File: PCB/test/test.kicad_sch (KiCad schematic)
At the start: 52 parts, among them CN1 HEADER_1X10, CN2 HEADER_1X10, CN3 USB_1, CN4 HEADER_1X4, CN5 UFL, SW2 MLL1200S_TE, U1 STM32WBxx_QFN48, U2 USBLC6-2SC6, U3 LD3985M33R, X1 NX2016_32MHz, X2 NX2012_32K768Hz

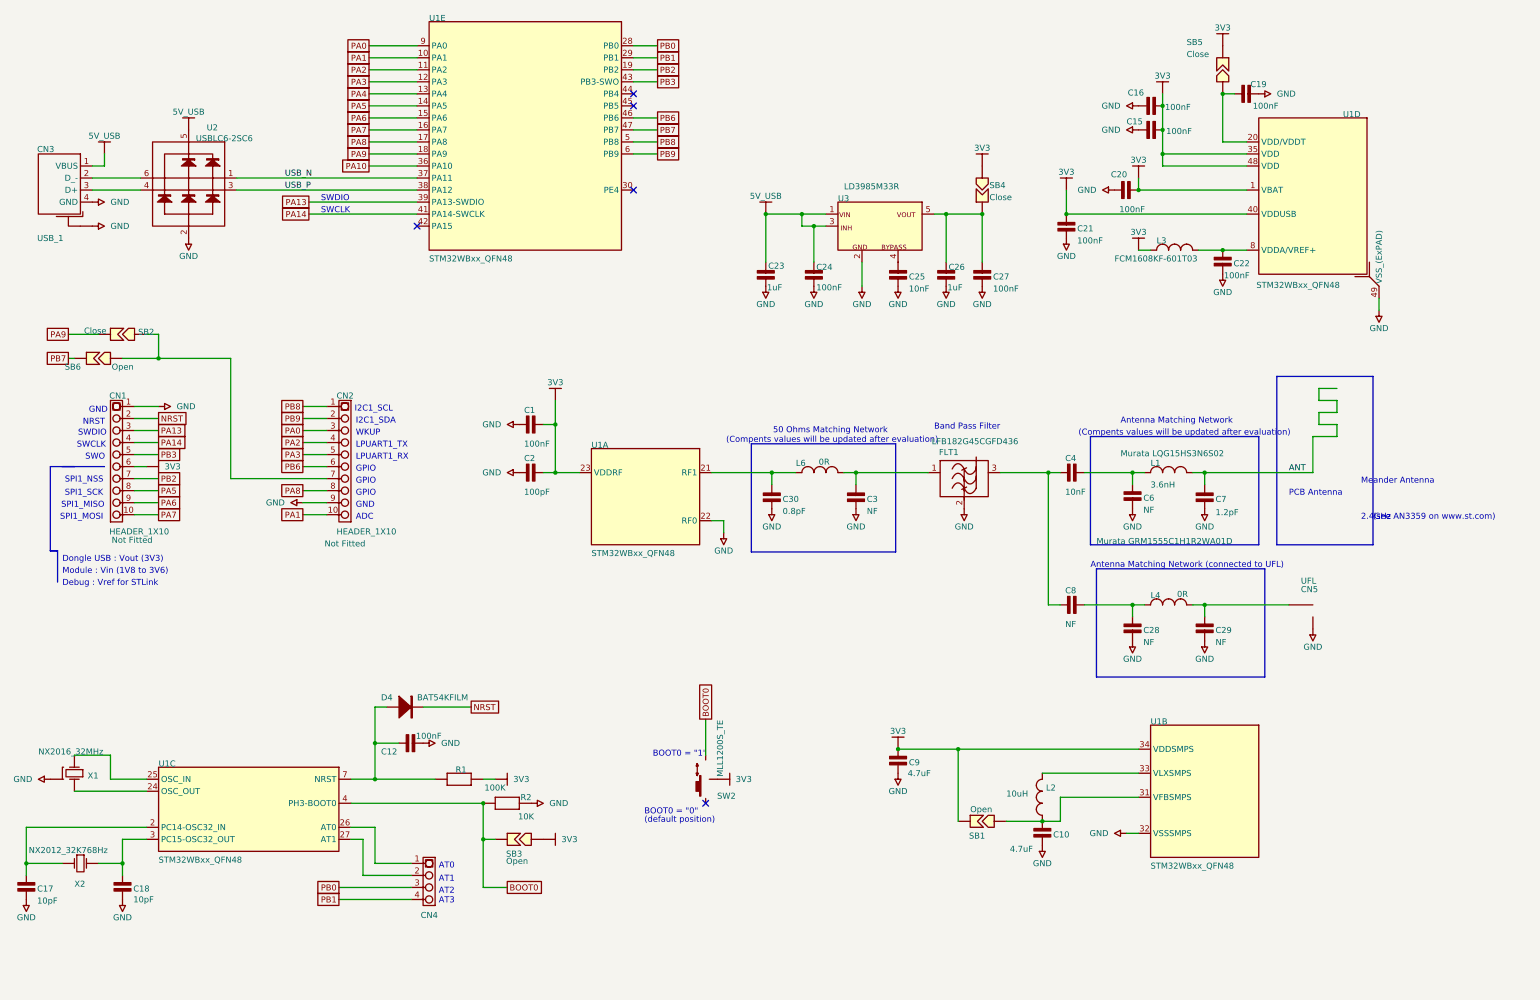
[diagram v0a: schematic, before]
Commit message: ajout de test
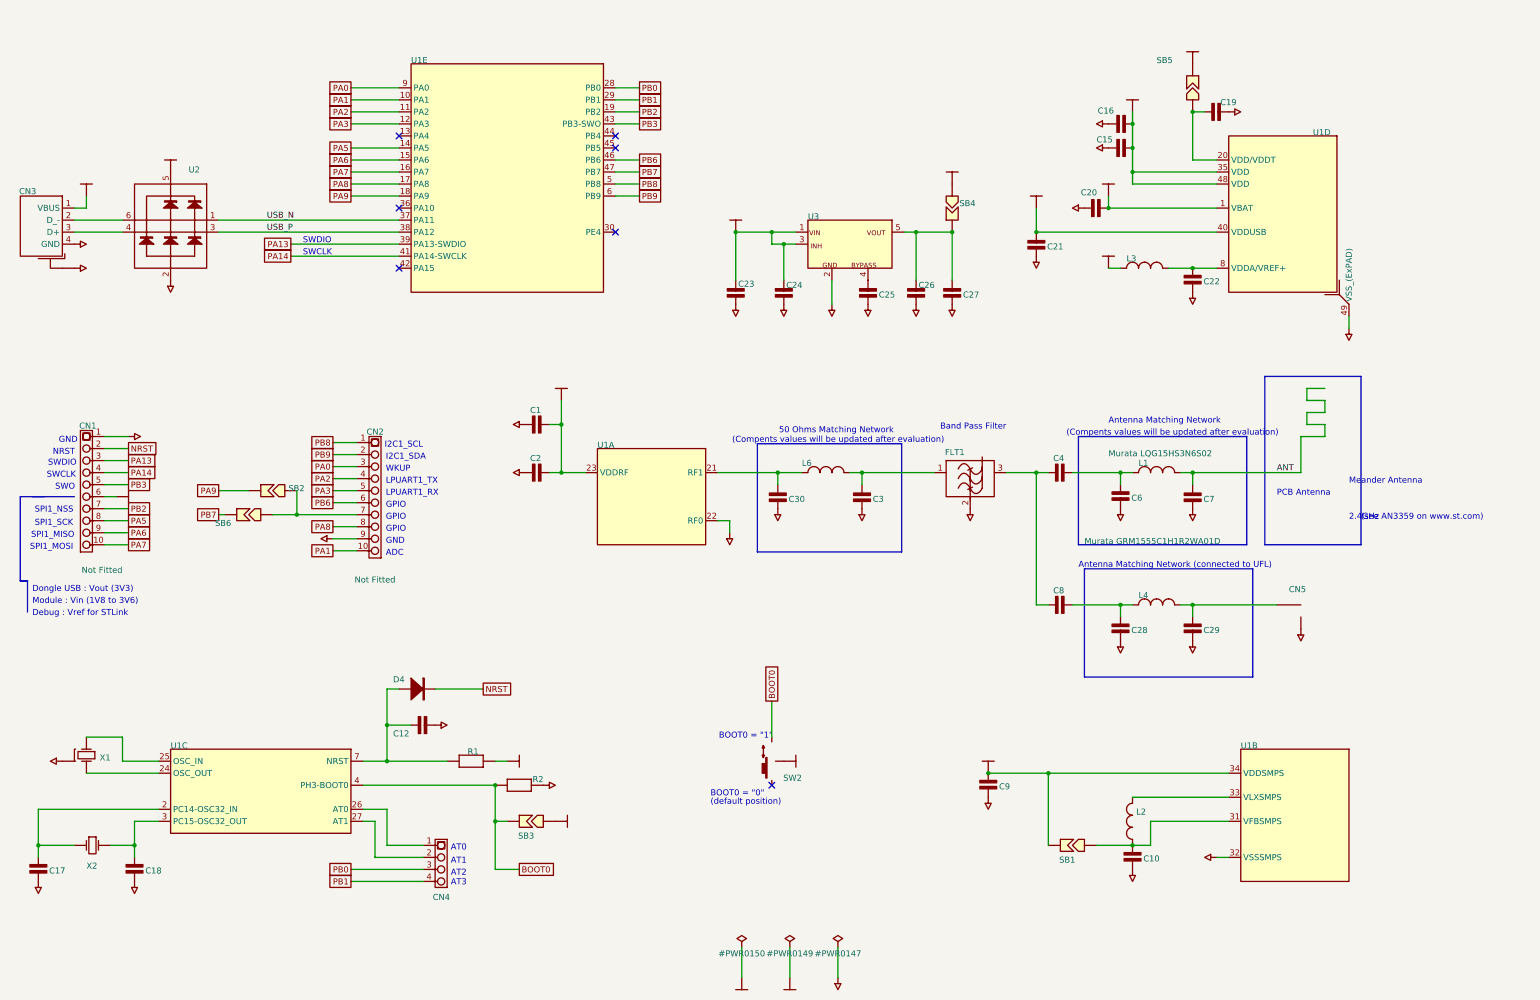
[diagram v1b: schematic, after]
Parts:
- removed C1, C12, C19, C20: 100nF, 0402_CAP_NPOL, symbol Schematic-altium-import:1_CAP_NPOL
- removed C10, C9: 4.7uF, 0402_CAP_NPOL, symbol Schematic-altium-import:0_CAP_NPOL
- removed C15, C16: 100nF, 0402_CAP_NPOL, symbol Schematic-altium-import:3_CAP_NPOL
- removed C17, C18: 10pF, 0402_CAP_NPOL, symbol Schematic-altium-import:0_CAP_NPOL
- removed C2: 100pF, 0402_CAP_NPOL, symbol Schematic-altium-import:1_CAP_NPOL
- removed C21, C24, C27: 100nF, 0402_CAP_NPOL, symbol Schematic-altium-import:2_CAP_NPOL
- removed C22: 100nF, 0402_CAP_NPOL, symbol Schematic-altium-import:0_CAP_NPOL
- removed C23, C26: 1uF, 0603_CAP_NPOL, symbol Schematic-altium-import:2_CAP_NPOL
- removed C25: 10nF, 0402_CAP_NPOL, symbol Schematic-altium-import:2_CAP_NPOL
- removed C28, C29, C6: NF, 0402_CAP_NPOL, symbol Schematic-altium-import:0_CAP_NPOL
- removed C3: NF, 0402_CAP_NPOL, symbol Schematic-altium-import:2_CAP_NPOL
- removed C30: 0.8pF, 0402_CAP_NPOL, symbol Schematic-altium-import:2_CAP_NPOL
- removed C4: 10nF, 0402_CAP_NPOL, symbol Schematic-altium-import:1_CAP_NPOL
- removed C7: 1.2pF, 0402_CAP_NPOL, symbol Schematic-altium-import:2_CAP_NPOL
- removed C8: NF, 0402_CAP_NPOL, symbol Schematic-altium-import:1_CAP_NPOL
- removed CN1: HEADER_1X10, Header M/F 1x10x2.54 NF, symbol Schematic-altium-import:0_HEADER_1X10
- removed CN2: HEADER_1X10, Header M/F 1x10x2.54 NF, symbol Schematic-altium-import:0_mirrored_HEADER_1X10
- removed CN3: USB_1, USB/A_M1, symbol Schematic-altium-import:0_USB_1
- removed CN4: HEADER_1X4, SIL4_127_B, symbol Schematic-altium-import:0_mirrored_HEADER_1X4
- removed CN5: UFL, UFL, symbol Schematic-altium-import:0_mirrored_UFL
- removed D4: BAT54KFILM, SOD523, symbol Schematic-altium-import:0_BAT54K
- removed FLT1: LFB182G45CGFD436, LFB182G45CGFD436, symbol Schematic-altium-import:0_LFB182G45CGFD436
- removed L1: 3.6nH, 0402_COIL, symbol Schematic-altium-import:1_INDUCTOR_SMD_STDL
- removed L2: 10uH, 0805_COIL, symbol Schematic-altium-import:2_IND_74479777310A
- removed L3: FCM1608KF-601T03, 0603_COIL, symbol Schematic-altium-import:1_IND_FCM1608KF-601T03
- removed L4, L6: 0R, 0402_COIL, symbol Schematic-altium-import:1_INDUCTOR_SMD_STDL
- removed R1: 100K, 0402_RES, symbol Schematic-altium-import:2_RES
- removed R2: 10K, 0402_RES, symbol Schematic-altium-import:0_RES
- removed SB1, SB3, SB6: Open, SB-tiny, symbol Schematic-altium-import:0_Strap2
- removed SB2: Close, SB-tiny, symbol Schematic-altium-import:0_Strap2
- removed SB4: Close, SB-tiny, symbol Schematic-altium-import:1_Strap2
- removed SB5: Close, SB-tiny, symbol Schematic-altium-import:3_Strap2
- removed SW2: MLL1200S_TE, MLL1200S_TE, symbol Schematic-altium-import:3_mirrored_MLL1200S_TE
- removed unit 5 of U1
- removed unit 4 of U1
- removed unit 3 of U1
- removed unit 1 of U1
- removed U2: USBLC6-2SC6, SOT23-6, symbol Schematic-altium-import:0_mirrored_USBLC6-2
- removed U3: LD3985M33R, SOT23-5, symbol Schematic-altium-import:0_LD3985M33R
- removed X1: NX2016_32MHz, NX2016_4P, symbol Schematic-altium-import:3_NX2016_32M
- removed X2: NX2012_32K768Hz, NX2012_2P, symbol Schematic-altium-import:0_NX2012_32K768
- added C1, C12, C19, C2, C20, C4, C8: (no value), symbol test-altium-import:1_CAP_NPOL
- added C10, C17, C18, C22, C28, C29, C6, C9: (no value), symbol test-altium-import:0_CAP_NPOL
- added C15, C16: (no value), symbol test-altium-import:3_CAP_NPOL
- added C21, C23, C24, C25, C26, C27, C30, C7: (no value), symbol test-altium-import:2_CAP_NPOL
- added CN1: (no value), symbol test-altium-import:0_HEADER_1X10
- added CN2: (no value), symbol test-altium-import:0_mirrored_HEADER_1X10
- added CN3: (no value), symbol test-altium-import:0_USB_1
- added CN4: (no value), symbol test-altium-import:0_mirrored_HEADER_1X4
- added CN5: (no value), symbol test-altium-import:0_mirrored_UFL
- added D4: (no value), symbol test-altium-import:0_BAT54K
- added FLT1: (no value), symbol test-altium-import:0_LFB182G45CGFD436
- added L1, L4, L6: (no value), symbol test-altium-import:1_INDUCTOR_SMD_STDL
- added L2: (no value), symbol test-altium-import:2_IND_74479777310A
- added L3: (no value), symbol test-altium-import:1_IND_FCM1608KF-601T03
- added R1: (no value), symbol test-altium-import:2_RES
- added R2: (no value), symbol test-altium-import:0_RES
- added SB1, SB2, SB3, SB6: (no value), symbol test-altium-import:0_Strap2
- added SB4: (no value), symbol test-altium-import:1_Strap2
- added SB5: (no value), symbol test-altium-import:3_Strap2
- added SW2: (no value), symbol test-altium-import:3_mirrored_MLL1200S_TE
- added U1: (no value), symbol test-altium-import:0_STM32WBxx_QFN48
- added U2: (no value), symbol test-altium-import:0_mirrored_USBLC6-2
- added U3: (no value), symbol test-altium-import:0_LD3985M33R
- added X1: (no value), symbol test-altium-import:3_NX2016_32M
- added X2: (no value), symbol test-altium-import:0_NX2012_32K768
- C3: renamed from U1; value STM32WBxx_QFN48 -> (none); footprint STM32WBxx_QFN48 -> (none); symbol Schematic-altium-import:0_STM32WBxx_QFN48 -> test-altium-import:2_CAP_NPOL
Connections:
- net 3V3: now also C1.2, C15.1, C16.1, C2.2, C20.2, C21.2, C9.1, CN1.6, L3.1, R1.1, SB1.2, SB3.1, SB4.1, SB5.2, SW2.2, U1.1 (VBAT), U1.23 (VDDRF), U1.34 (VDDSMPS), U1.35 (VDD), U1.40 (VDDUSB), U1.48 (VDD); no longer C3.34 (VDDSMPS)
- net 5V_USB: now also C23.2, C24.2, CN3.1 (VBUS), U2.5, U3.1 (VIN), U3.3 (CE)
- net ANT: now also C7.2, L1.2
- net BOOT0: now also R2.1, SB3.2, SW2.3, U1.4 (PH3-BOOT0)
- net GND: now also C3.1, C1.1, C10.2, C12.2, C15.2, C16.2, C17.2, C18.2, C19.2, C2.1, C20.1, C21.1, C22.2, C23.1, C24.1, C25.1, C26.1, C27.1, C28.2, C29.2, C30.1, C6.2, C7.1, C9.2, CN1.1, CN2.9, CN3.0 (Shield), CN3.4 (GND), CN5.2 (Y), FLT1.2 (GND), R2.2, U1.22 (RF0), U1.32 (VSSSMPS), U1.49 (VSS_(ExPAD)), U2.2, U3.2 (VSS), X1.2, X1.4; no longer C3.32 (VSSSMPS)
- net NRST: now also CN1.2, D4.K
- net PA0: now also CN2.3, U1.9 (PA0)
- net PA1: now also CN2.10, U1.10 (PA1)
- net PA13: now also CN1.3, U1.39 (PA13-SWDIO)
- net PA14: now also CN1.4, U1.41 (PA14-SWCLK)
- net PA2: now also CN2.4, U1.11 (PA2)
- net PA3: now also CN2.5, U1.12 (PA3)
- net PA5: now also CN1.8, U1.14 (PA5)
- net PA6: now also CN1.9, U1.15 (PA6)
- net PA7: now also CN1.10, U1.16 (PA7)
- net PA8: now also CN2.8, U1.17 (PA8)
- net PA9: now also SB2.2, U1.18 (PA9)
- net PB0: now also CN4.3, U1.28 (PB0)
- net PB1: now also CN4.4, U1.29 (PB1)
- net PB2: now also CN1.7, U1.19 (PB2)
- net PB3: now also CN1.5, U1.43 (PB3-SWO)
- net PB6: now also CN2.6, U1.46 (PB6)
- net PB7: now also SB6.2, U1.47 (PB7)
- net PB8: now also CN2.1, U1.5 (PB8)
- net PB9: now also CN2.2, U1.6 (PB9)
- net USB_N: now also U1.37 (PA11), U2.1
- net USB_P: now also U1.38 (PA12), U2.3
- new net: C29.1, CN5.1 (X), L4.2
- new net: C10.1, L2.1, SB1.1, U1.31 (VFBSMPS)
- new net: CN4.1, U1.26 (AT0)
- new net: CN4.2, U1.27 (AT1)
- new net: C3.2, FLT1.1 (I/O), L6.2
- new net: C4.1, C8.1, FLT1.3 (I/O)
- new net: C28.1, C8.2, L4.1
- new net: C19.1, SB5.1, U1.20 (VDD/VDDT)
- new net: C30.2, L6.1, U1.21 (RF1)
- new net: U1.25 (OSC_IN), X1.1 (OSC1)
- new net: U1.24 (OSC_OUT), X1.3 (OSC2)
- new net: C4.2, C6.1, L1.1
- new net: C17.1, U1.2 (PC14-OSC32_IN), X2.1 (OSC1)
- new net: C18.1, U1.3 (PC15-OSC32_OUT), X2.2 (OSC2)
- new net: C12.1, D4.A, R1.2, U1.7 (NRST)
- new net: L2.2, U1.33 (VLXSMPS)
- new net: C26.2, C27.2, SB4.2, U3.5 (VOUT)
- new net: C22.1, L3.2, U1.8 (VDDA/VREF+)
- new net: CN3.3 (D+), U2.4
- new net: CN3.2 (D_-), U2.6
- new net: CN2.7, SB2.1, SB6.1
- new net: C25.2, U3.4 (BYPASS)
- no-connect marks 5 -> 7

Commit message: ajout buzzer + oxymètre
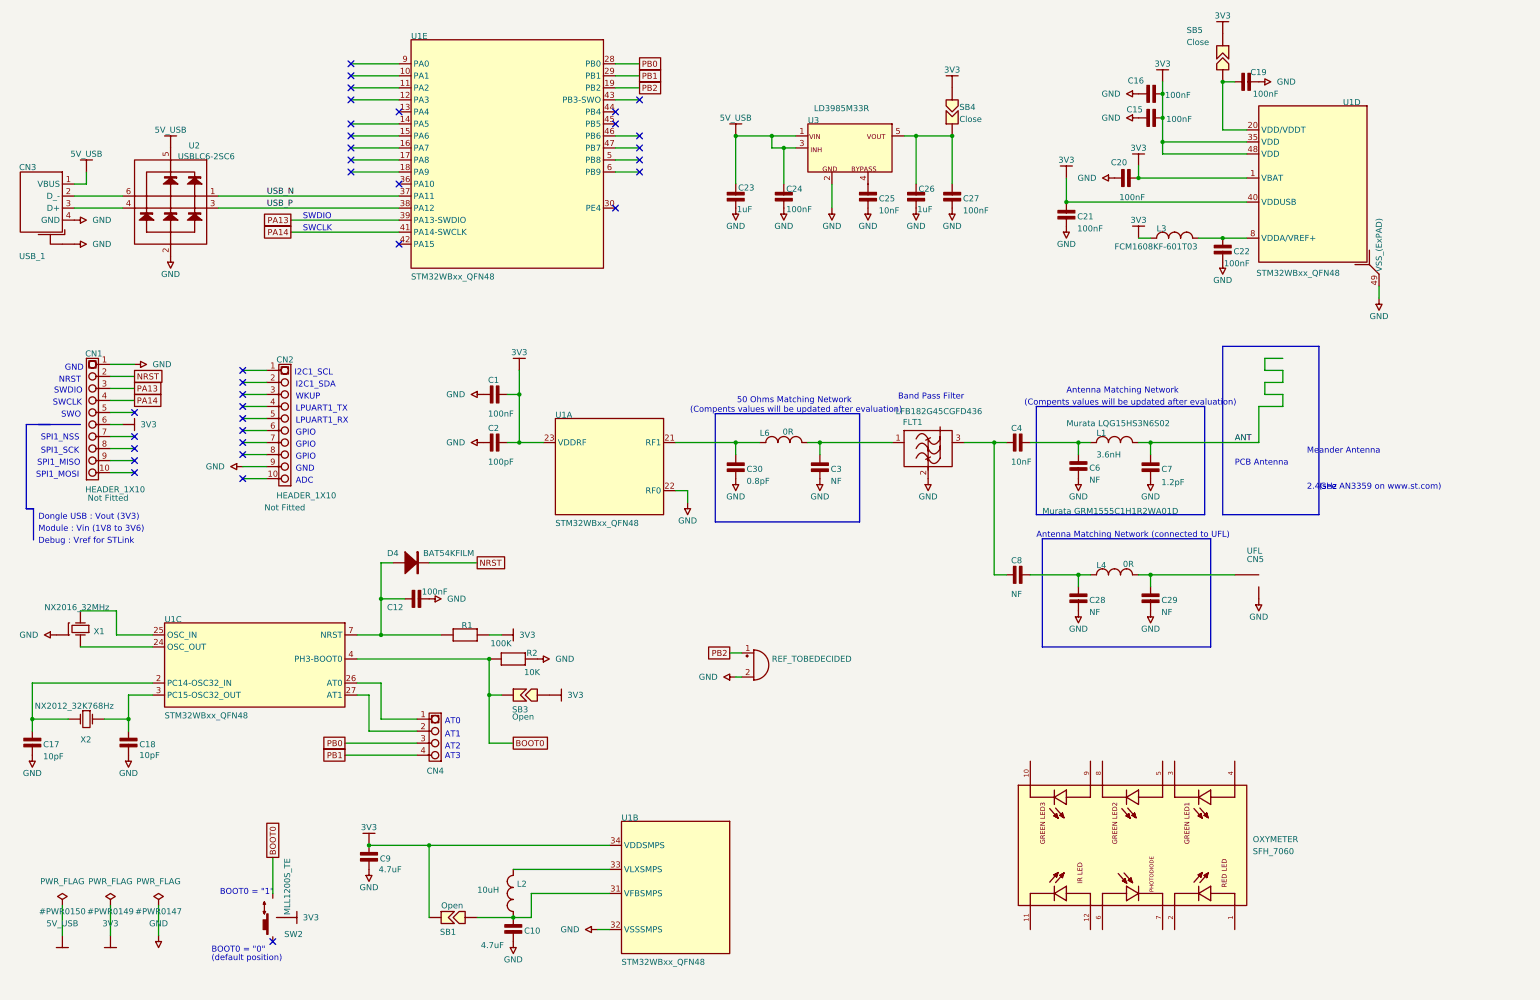
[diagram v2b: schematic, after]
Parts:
- removed SB2, SB6: (no value), symbol test-altium-import:0_Strap2
- added OXYMETER: SFH_7060, XDCR_SFH_7060, symbol SFH_7060:SFH_7060
- added REF_TOBEDECIDED: (no value), symbol Device:Buzzer
- C1, C12, C15, C16, C19, C20, C21, C22, C24, C27: value (none) -> 100nF; footprint (none) -> 0402_CAP_NPOL
- C10, C9: value (none) -> 4.7uF; footprint (none) -> 0402_CAP_NPOL
- C17, C18: value (none) -> 10pF; footprint (none) -> 0402_CAP_NPOL
- C2: value (none) -> 100pF; footprint (none) -> 0402_CAP_NPOL
- C23, C26: value (none) -> 1uF; footprint (none) -> 0603_CAP_NPOL
- C25, C4: value (none) -> 10nF; footprint (none) -> 0402_CAP_NPOL
- C28, C29, C3, C6, C8: value (none) -> NF; footprint (none) -> 0402_CAP_NPOL
- C30: value (none) -> 0.8pF; footprint (none) -> 0402_CAP_NPOL
- C7: value (none) -> 1.2pF; footprint (none) -> 0402_CAP_NPOL
- CN1, CN2: value (none) -> HEADER_1X10; footprint (none) -> Header M/F 1x10x2.54 NF
- CN3: value (none) -> USB_1; footprint (none) -> USB/A_M1
- CN4: value (none) -> HEADER_1X4; footprint (none) -> SIL4_127_B
- CN5: value (none) -> UFL; footprint (none) -> UFL
- D4: value (none) -> BAT54KFILM; footprint (none) -> SOD523
- FLT1: value (none) -> LFB182G45CGFD436; footprint (none) -> LFB182G45CGFD436
- L1: value (none) -> 3.6nH; footprint (none) -> 0402_COIL
- L2: value (none) -> 10uH; footprint (none) -> 0805_COIL
- L3: value (none) -> FCM1608KF-601T03; footprint (none) -> 0603_COIL
- L4, L6: value (none) -> 0R; footprint (none) -> 0402_COIL
- R1: value (none) -> 100K; footprint (none) -> 0402_RES
- R2: value (none) -> 10K; footprint (none) -> 0402_RES
- SB1, SB3: value (none) -> Open; footprint (none) -> SB-tiny
- SB4, SB5: value (none) -> Close; footprint (none) -> SB-tiny
- SW2: value (none) -> MLL1200S_TE; footprint (none) -> MLL1200S_TE
- U1: value (none) -> STM32WBxx_QFN48; footprint (none) -> STM32WBxx_QFN48
- U2: value (none) -> USBLC6-2SC6; footprint (none) -> SOT23-6
- U3: value (none) -> LD3985M33R; footprint (none) -> SOT23-5
- X1: value (none) -> NX2016_32MHz; footprint (none) -> NX2016_4P
- X2: value (none) -> NX2012_32K768Hz; footprint (none) -> NX2012_2P
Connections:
- net GND: now also REF_TOBEDECIDED.2 (+)
- net PB2: now also REF_TOBEDECIDED.1 (-); no longer CN1.7
- net PA0: no longer names the net of U1.9 (PA0)
- net PA0: no longer CN2.3
- net PA1: no longer names the net of U1.10 (PA1)
- net PA1: no longer CN2.10
- net PA2: no longer names the net of U1.11 (PA2)
- net PA2: no longer CN2.4
- net PA3: no longer names the net of U1.12 (PA3)
- net PA3: no longer CN2.5
- net PA5: no longer names the net of U1.14 (PA5)
- net PA5: no longer CN1.8
- net PA6: no longer names the net of U1.15 (PA6)
- net PA6: no longer CN1.9
- net PA7: no longer names the net of U1.16 (PA7)
- net PA7: no longer CN1.10
- net PA8: no longer names the net of U1.17 (PA8)
- net PA8: no longer CN2.8
- net PA9: no longer names the net of U1.18 (PA9)
- net PB3: no longer names the net of U1.43 (PB3-SWO)
- net PB3: no longer CN1.5
- net PB6: no longer names the net of U1.46 (PB6)
- net PB6: no longer CN2.6
- net PB7: no longer names the net of U1.47 (PB7)
- net PB8: no longer names the net of U1.5 (PB8)
- net PB8: no longer CN2.1
- net PB9: no longer names the net of U1.6 (PB9)
- net PB9: no longer CN2.2
- no-connect marks 7 -> 35
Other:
- moved on the sheet: C1, C10, C12, C15, C16, C17, C18, C19, C2, C20, C21, C22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

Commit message: schema quasi fini
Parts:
- removed REF_TOBEDECIDED: (no value), symbol Device:Buzzer
- added BUTTON1: (no value), symbol MPB02-1B00-R-D:MPB02-1B00-R-D
- added BUTTON2, BUTTON3: MPB02-1B00-R-D, SW_MPB02-1B00-R-D, symbol MPB02-1B00-R-D:MPB02-1B00-R-D
- added BUZZER1: CMT-4023S-SMT-TR, CUI_CMT-4023S-SMT-TR, symbol CMT-4023S-SMT-TR:CMT-4023S-SMT-TR
- added FIXATION_ECRAN1: (no value), symbol test-altium-import:0_mirrored_HEADER_1X4
- added R_BUTTONS1: (no value), symbol Device:R
- renumbered OXYMETER to OXYMETER1
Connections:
- net 3V3: now also R_BUTTONS1.2
- net GND: now also OXYMETER1.10, OXYMETER1.11, OXYMETER1.2, OXYMETER1.3, OXYMETER1.8, BUZZER1.N, FIXATION_ECRAN1.1
- net PB2: now also BUZZER1.P
- net PA1: now reaches U1.10 (PA1)
- net PA1: now also OXYMETER1.5
- net PA2: now reaches U1.11 (PA2)
- net PA2: now also OXYMETER1.4
- net PA3: now reaches U1.12 (PA3)
- net PA3: now also OXYMETER1.12
- net PA4: now reaches U1.13 (PA4)
- net PA4: now also OXYMETER1.1
- net PA5: now reaches U1.14 (PA5)
- net PA5: now also OXYMETER1.6
- net PA6: now reaches U1.15 (PA6)
- net PA6: now also OXYMETER1.7
- net PA7: now reaches U1.16 (PA7)
- net PA7: now also BUTTON2.3
- net PA8: now reaches U1.17 (PA8)
- net PA8: now also BUTTON1.3
- net PA9: now reaches U1.18 (PA9)
- net PA9: now also BUTTON3.3
- net at U1.44 (PB4): now also FIXATION_ECRAN1.2
- net at U1.45 (PB5): now also FIXATION_ECRAN1.3
- net at U1.46 (PB6): now also FIXATION_ECRAN1.4
- net PA0: now reaches U1.9 (PA0)
- net PA0: now also OXYMETER1.9
- new net: BUTTON1.1, BUTTON2.1, BUTTON3.1, R_BUTTONS1.1
- no-connect marks 35 -> 22
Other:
- moved on the sheet: C23, C24, C25, C26, C27, OXYMETER1, SB4, U3

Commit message: suppression pins
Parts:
- removed CN2: HEADER_1X10, Header M/F 1x10x2.54 NF, symbol test-altium-import:0_mirrored_HEADER_1X10
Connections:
- net 3V3: no longer CN1.6
- net PA13: no longer names the net of U1.39 (PA13-SWDIO)
- net PA13: no longer CN1.3
- net PA14: no longer names the net of U1.41 (PA14-SWCLK)
- net PA14: no longer CN1.4
- no-connect marks 22 -> 18
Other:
- note removed: "ADC"
- note removed: "GPIO"
- note removed: "I2C1_SCL"
- note removed: "I2C1_SDA"
- note removed: "LPUART1_RX"
- note removed: "LPUART1_TX"
- note removed: "WKUP"
- moved on the sheet: C23, C24, C25, C26, C27, SB4, U3
